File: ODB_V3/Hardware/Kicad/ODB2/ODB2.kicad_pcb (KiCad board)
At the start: 4 copper layers, 63.5 x 127 mm, 243 parts, among them IC1 W25Q512JVEIQ, J1 1715310000, J10 GPS_Conn_02x04_Top_Bottom, J15 Vin_XT30PW-F, J2 RFD_GT17HN-4DP-2HA56, J3 SYS_SW_Conn_01x05_Header, J5 MEM2067, J6 IdeFIX_GT17HN-4DP-2HA56, J7 1715250000, J8 1715310000, J9 1715250000, U1 STM32F412ZGTx, U10 ADXL382-2BCCZ-RL7, U11 SI5442DU-T1-GE3, U12 SI5442DU-T1-GE3, U13 L6981N33DR, U2 LM339, U3 SI5442DU-T1-GE3, U4 MS580301BA01-00, U6 BNO055, U7 MPQ9843GLE-5-AEC1-Z, U8 SI5442DU-T1-GE3, U9 MAX6612MXK, Y1 ABM8G-25.000MHZ-18-D2Y-T

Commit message: WIP: Initial rough placement of circuit blocks on PCB
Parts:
- moved PA_Q1 309.0 mm to (-7.54, 79.6)
- moved PA_Q2 309.0 mm to (-7.54, 84.2)
- moved PA_Q3 309.0 mm to (-16.7, 92.5)
- moved PA_R1 309.0 mm to (-17.0, 78.2)
- moved PA_R2 309.0 mm to (-17.0, 80.7)
- moved PA_R3 309.0 mm to (-17.0, 83.2)
- moved PA_R4 309.0 mm to (-17.0, 85.7)
- moved PA_R5 309.0 mm to (-17.0, 88.2)
- moved Vin_C1 309.0 mm to (-12.0, 83.5)
- moved Vin_R3 309.0 mm to (-12.0, 86.0)
- moved Vin_R4 309.0 mm to (-12.0, 88.5)
- moved Vin_C2 285.2 mm to (-7.67, 126.9)
- moved Vin_C5 285.2 mm to (-7.67, 131.1)
- moved Vin_C6 285.2 mm to (-7.67, 135.4)
- moved Vin_C7 285.2 mm to (-2.72, 133.5)
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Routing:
- net Net-(J15-PadP): track 0.00 -> 26.5 mm
- net 5V_Main: track 28.0 -> 10.2 mm
- net Net-(U7-VCC): track 13.9 -> 5.22 mm

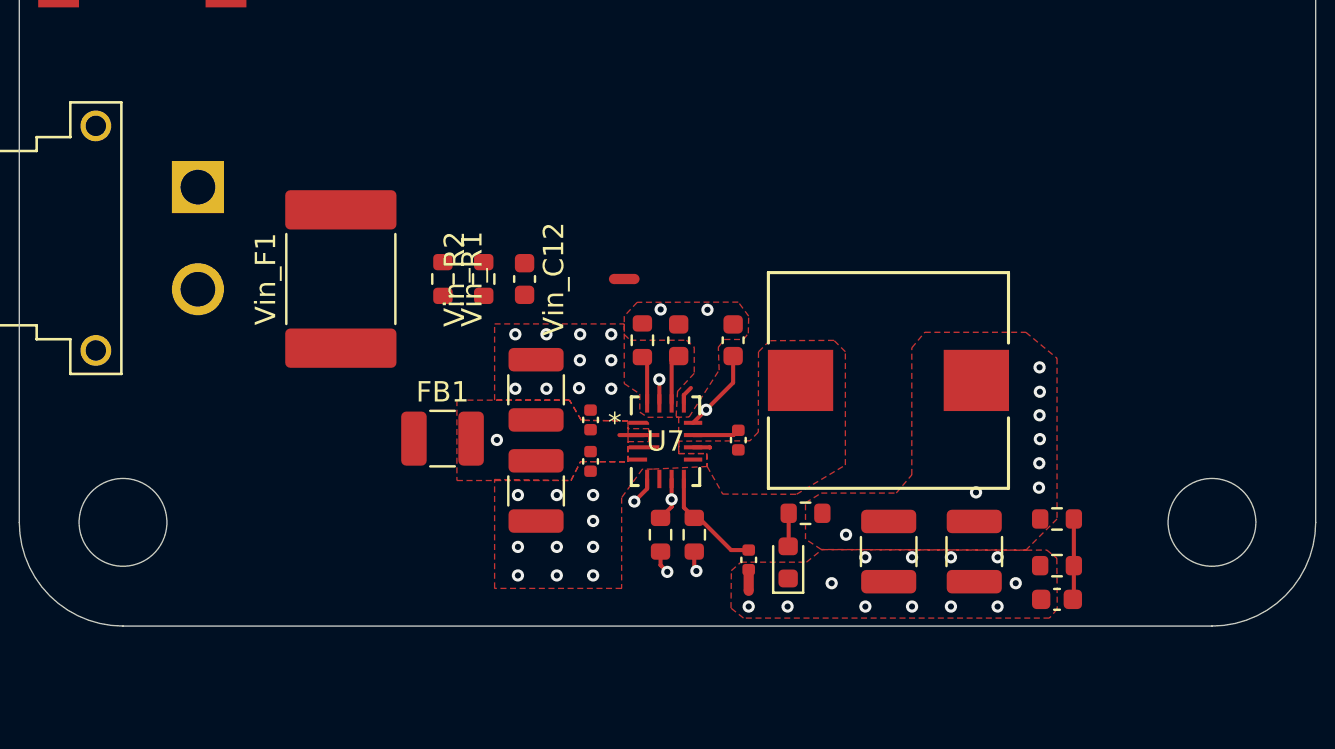
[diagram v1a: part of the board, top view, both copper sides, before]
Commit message: fix : Buck 5V traces and powerplane isolation
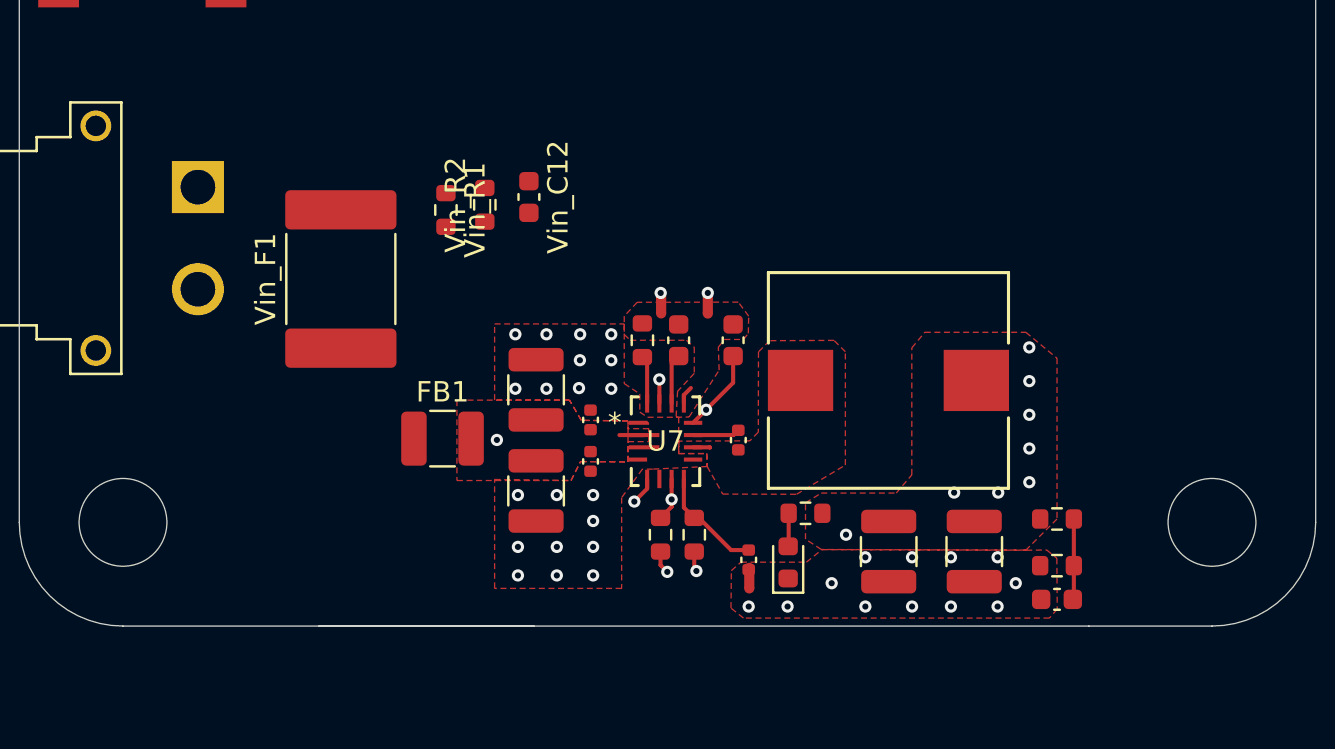
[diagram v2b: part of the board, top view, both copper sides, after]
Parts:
- added NT5: NetTie_2, NetTie:NetTie-2_SMD_Pad0.5mm, F.Cu at (51.7, 131.2)
- moved NT1 15.9 mm to (56.0, 144.7), turned to -90 degrees
- moved NT2 13.7 mm to (54.0, 131.2), turned to 90 degrees
- moved Vin_C12 4.02 mm to (45.2, 126.0)
- moved Vin_R2 3.64 mm to (43.1, 126.4)
- moved Vin_R1 3.38 mm to (41.1, 126.6)
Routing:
- net Net-(J15-PadP): track 26.5 -> 0.00 mm
- net 5V_Main: track 10.2 -> 27.0 mm
- net Net-(U7-VCC): track 5.22 -> 13.9 mm
- net GND: vias 32 -> 34
- net AGND5V: vias 2 -> 0
- added copper zone on In2.Cu, net 5V_Main
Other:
- outline, holes or cut-outs redrawn

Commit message: wip: 3v3 buck
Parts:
- removed NT3: NetTie_2, NetTie:NetTie-2_SMD_Pad0.5mm
- removed TP14, TP21: TestPoint, TestPoint:TestPoint_Pad_D1.0mm
- 3V3_C1, 3V3_C10, 3V3_C2: footprint Capacitor_SMD:C_1210_3225Metric -> Capacitor_SMD:C_0603_1608Metric
- NT4: footprint NetTie:NetTie-2_SMD_Pad0.5mm -> NetTie:NetTie-4_SMD_Pad0.5mm
- moved Vin_C6 56.4 mm to (47.5, 123.5), turned to 90 degrees
- moved Vin_C5 55.2 mm to (47.5, 129.5), turned to -90 degrees
- moved 3V3_LED1 52.9 mm to (61.8, 114.0), turned to 90 degrees
- moved Vin_C4 52.8 mm to (54.8, 123.2), turned to 90 degrees
- moved NT4 51.8 mm to (77.8, 108.0), turned to 90 degrees
- moved FB2 49.4 mm to (70.8, 110.8)
- moved Vin_C2 47.0 mm to (39.2, 128.8), turned to 180 degrees
- moved U13 46.3 mm to (77.4, 111.5), turned to 180 degrees
- moved 3V3_R3 41.3 mm to (67.8, 113.2)
- moved 3V3_C8 40.7 mm to (65.2, 126.5), turned to 180 degrees
- moved Vin_C7 38.5 mm to (35.5, 128.8), turned to -90 degrees
- moved 3V3_C3 37.3 mm to (71.5, 108.2), turned to 180 degrees
- moved Vin_C8 36.9 mm to (33.5, 128.8), turned to -90 degrees
- moved 3V3_C7 36.4 mm to (65.2, 116.0), turned to 180 degrees
- moved 3V3_R1 34.6 mm to (78.8, 131.0), turned to 90 degrees
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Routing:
- net GND: track 0.00 -> 13.7 mm, vias 34 -> 109
- net Net-(3V3_LED1-A): track 0.00 -> 5.19 mm
- net 3V3_An: track 0.00 -> 4.43 mm
- net AGND3V3: track 0.00 -> 4.28 mm
- net Net-(U13-VCC): track 0.00 -> 2.09 mm
- net Net-(U13-BOOT): track 0.00 -> 1.77 mm
- net 3V3_Main: vias 0 -> 27
- added copper zone on F.Cu, net 3V3_Main
- added copper zone on In2.Cu, net 3V3_Main
- added copper zone on F.Cu, net AGND3V3
- added copper zone on B.Cu, net GND
- added copper zone on F.Cu, net Net-(J15-PadP)
- added copper zone on F.Cu, net Net-(U13-EN/CLKIN)
- added copper zone on F.Cu, net Net-(U13-SW)
- added copper zone on F.Cu, net VIN_Filtered

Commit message: wip: pyro1 & pyro2
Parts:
- moved P_R13 15.9 mm to (32.0, 44.6), turned to 90 degrees
- moved P_C6 15.0 mm to (32.0, 50.4)
- moved P_R14 12.3 mm to (33.6, 44.6), turned to 90 degrees
- moved U3 10.1 mm to (33.1, 37.4), turned to 90 degrees
- moved P_D2 9.63 mm to (33.8, 40.5), turned to 90 degrees
- moved P_C7 9.00 mm to (35.2, 44.6)
- moved P_C3 7.08 mm to (32.0, 40.4), turned to -90 degrees
- moved P_C2 5.94 mm to (35.2, 34.5), turned to -90 degrees
- moved P_R15 5.92 mm to (35.6, 50.4), turned to 90 degrees
- moved P_D1 5.65 mm to (36.9, 34.6), turned to 90 degrees
- moved P_D6 5.39 mm to (33.8, 50.5), turned to 90 degrees
- moved P_D5 3.69 mm to (36.9, 44.7), turned to 90 degrees
- moved U11 3.64 mm to (33.1, 47.5), turned to 90 degrees
- moved P_R5 3.09 mm to (32.0, 34.5), turned to 90 degrees
- moved P_R6 2.45 mm to (33.6, 34.5), turned to 90 degrees
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
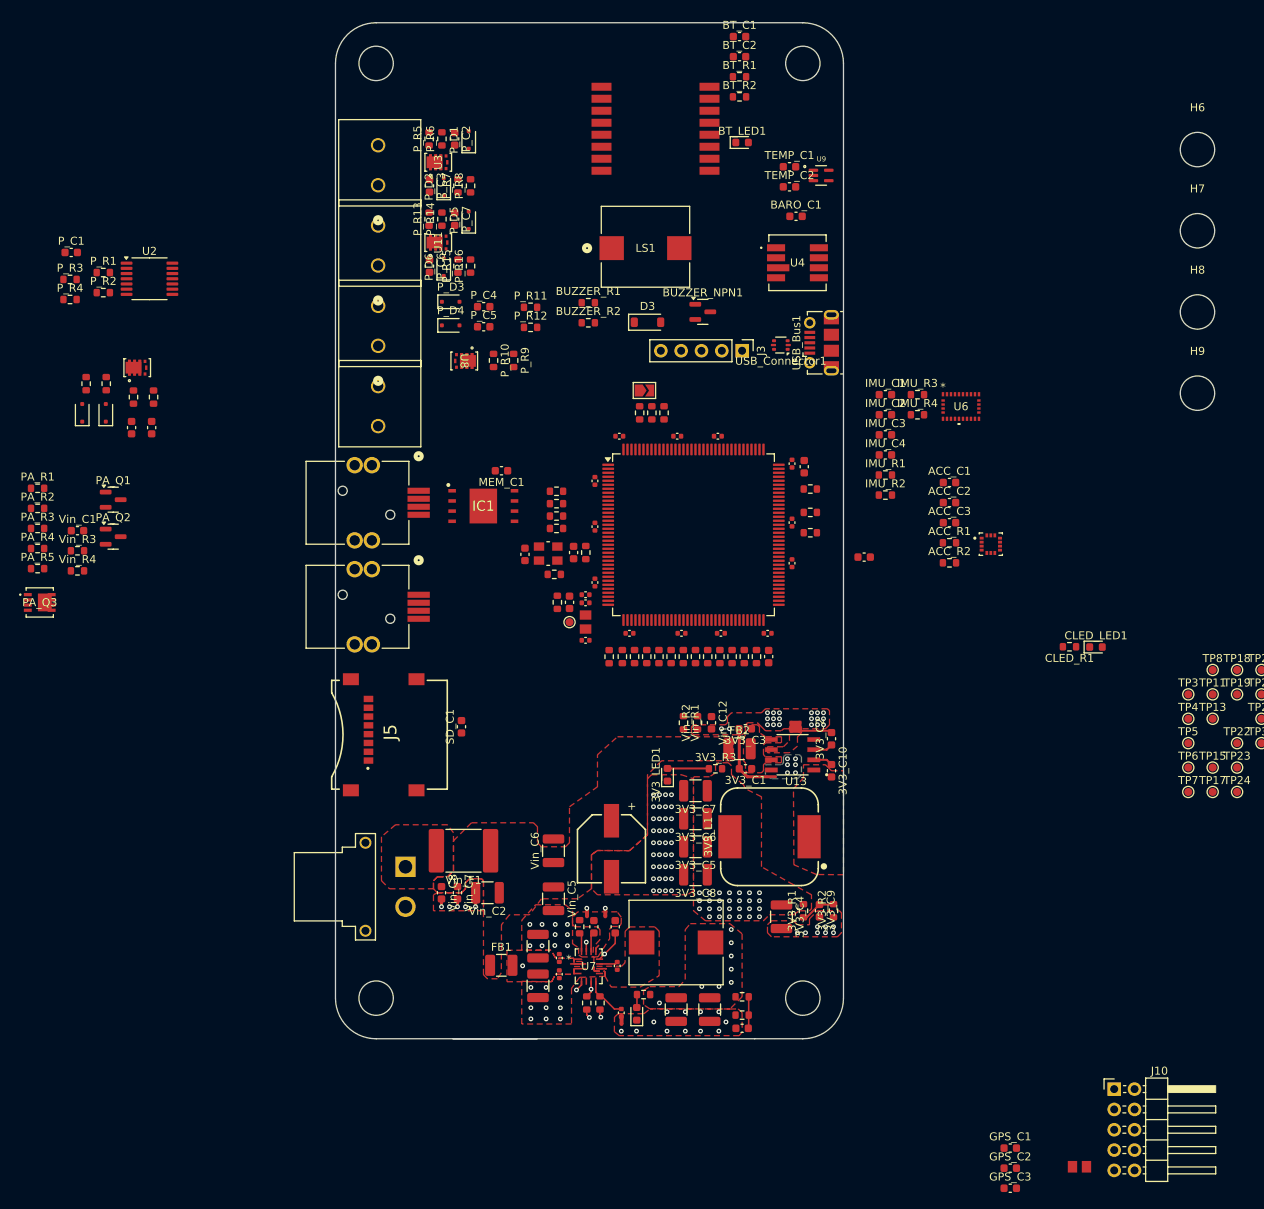
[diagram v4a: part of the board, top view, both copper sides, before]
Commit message: WIP : Layout brouillon complet, fix pyro armement
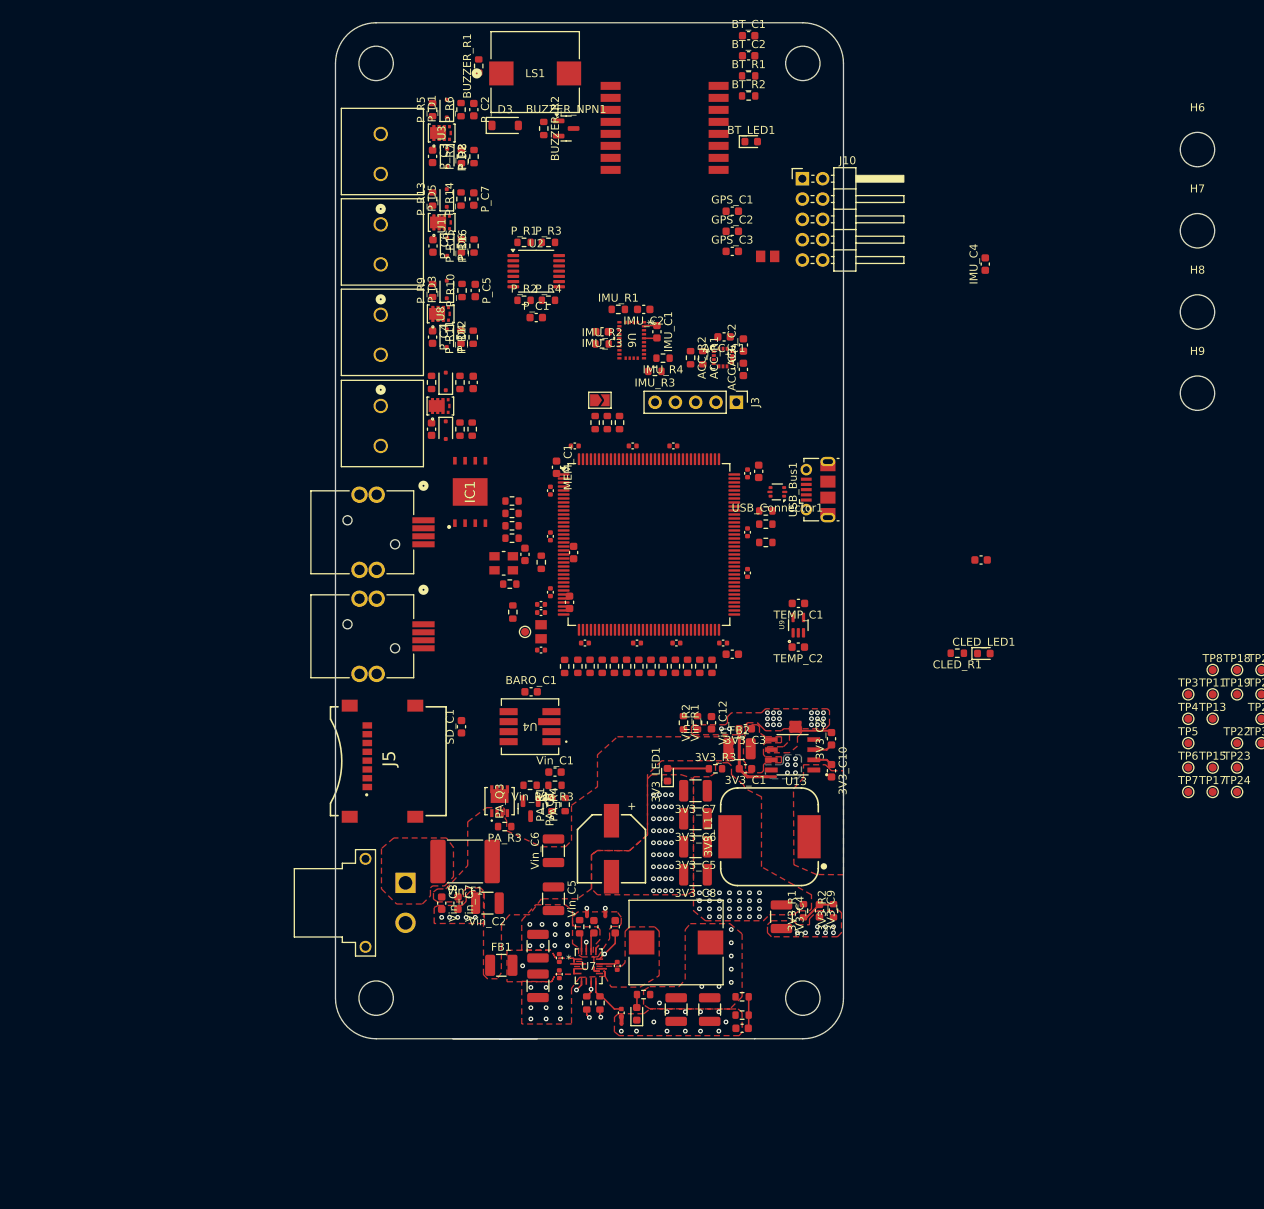
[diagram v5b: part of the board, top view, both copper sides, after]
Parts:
- removed PA_Q2: MMBTA94, Package_TO_SOT_SMD:SOT-23
- removed PA_R2: 10k, Resistor_SMD:R_0603_1608Metric
- removed PA_R5: 1.5k, Resistor_SMD:R_0603_1608Metric
- moved GPS_C1 122.2 mm to (69.8, 43.6)
- moved GPS_C2 122.2 mm to (69.8, 46.1)
- moved GPS_C3 122.2 mm to (69.8, 48.6)
- moved GPS_FB1 120.3 mm to (74.3, 49.2)
- moved J10 120.3 mm to (78.6, 39.5)
- moved PA_R1 75.5 mm to (47.3, 117.7), turned to 90 degrees
- moved PA_R4 73.3 mm to (49.0, 117.7), turned to 90 degrees
- moved PA_R3 69.3 mm to (41.4, 120.5), turned to 180 degrees
- moved BARO_C1 68.0 mm to (44.7, 103.6)
- moved U4 66.9 mm to (44.6, 108.0), turned to 180 degrees
- moved Vin_C1 66.9 mm to (47.7, 113.7)
- moved Vin_R3 66.5 mm to (47.7, 115.3), turned to 180 degrees
- moved PA_Q1 64.9 mm to (44.6, 118.2), turned to -90 degrees
- moved PA_Q3 62.6 mm to (40.8, 117.3), turned to 90 degrees
- moved Vin_R4 62.6 mm to (44.6, 115.3), turned to 180 degrees
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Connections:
- NT4 pad 3: AGND3V3 -> (no net)
- NT4 pad 4: GND -> (no net)
- PA_R4 pad 1: Net-(PA_Q2-B) -> Net-(PA_Q1-B)
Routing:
- net GND: track 13.7 -> 11.6 mm
- net 3V3_Main: track 0.00 -> 1.66 mm
